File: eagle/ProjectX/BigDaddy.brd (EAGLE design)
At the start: 100 x 100 mm, 4 parts, among them U1 TC4427AEOA

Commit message: Working on the big board
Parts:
- added C1, C3, C5, C6: (no value), resistor:C0805
- added SP10, SP11, SP12, SP5, SP6, SP9: MA40S4S, Parts:MA40
- added U3, U5, U6: TC4427AEOA, Parts:SOIC127P600X175-8N
- moved U1 42.1 mm to (38.5, 36.0)
- moved SP1 41.4 mm to (43.0, 36.0), flipped to the bottom
- moved SP2 40.5 mm to (31.0, 36.0), flipped to the bottom
- moved DIP1 16.2 mm to (49.0, 54.0)
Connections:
- new net N$10: SP6.+, U3.5
- new net N$13: SP11.+, U6.7
- new net N$14: SP12.+, U6.5
- new net N$7: SP9.+, U5.7
- new net N$8: SP10.+, U5.5
- new net N$9: SP5.+, U3.7
- new net VDD: C1.2, C3.2, C5.2, C6.2, U1.6, U3.6, U5.6, U6.6
- net +5V: no longer U1.6
- net GND: now also C1.1, C3.1, C5.1, C6.1, SP10.-, SP11.-, SP12.-, SP5.-, SP6.-, SP9.-, U3.3, U5.3, U6.3
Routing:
- net GND: track 0.00 -> 32.1 mm, vias 0 -> 1
- net VDD: track 0.00 -> 26.8 mm, vias 0 -> 4
- net N$9: track 0.00 -> 8.37 mm
- net N$13: track 0.00 -> 7.58 mm
- net N$2: track 0.00 -> 5.73 mm
- net N$8: track 0.00 -> 4.73 mm
- added copper zone on layer 1, net GND
- added copper zone on layer 16, net VDD

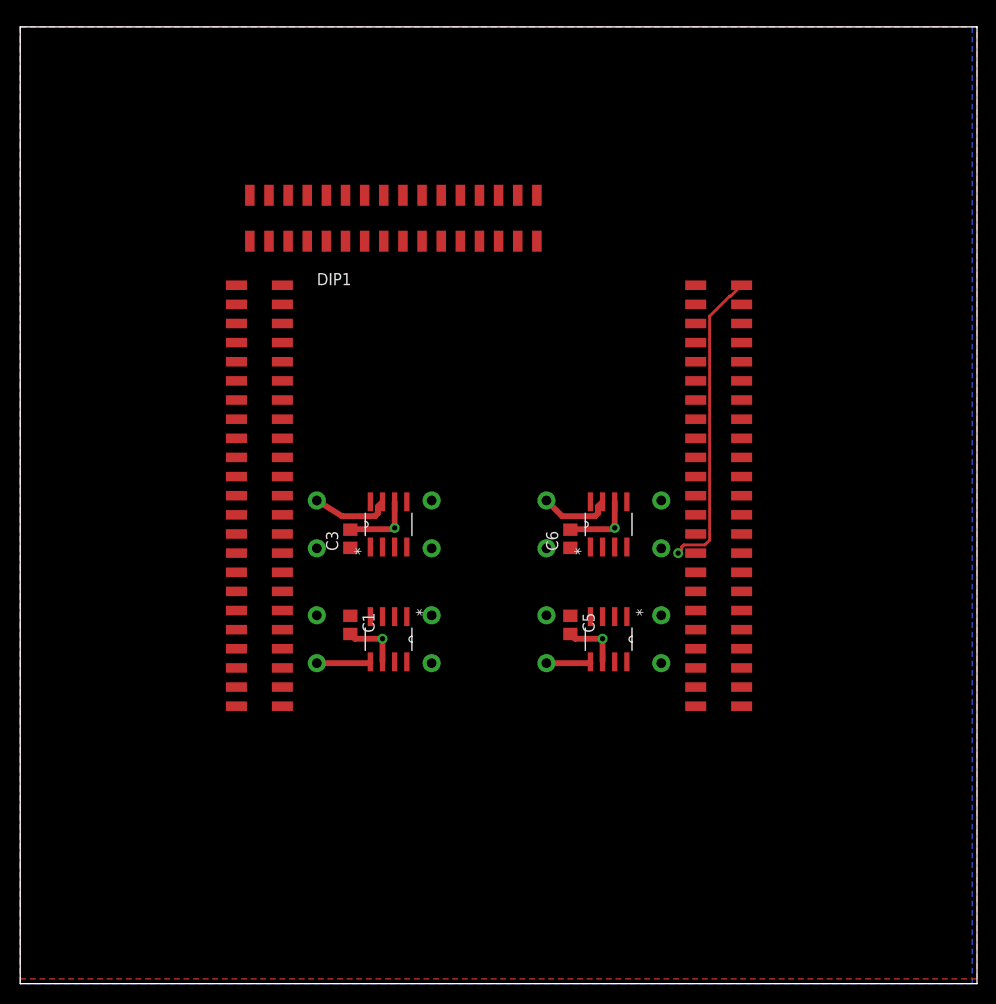
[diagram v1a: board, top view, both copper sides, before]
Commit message: Layout of transducers complete, need to add connectors, power, and then route everything
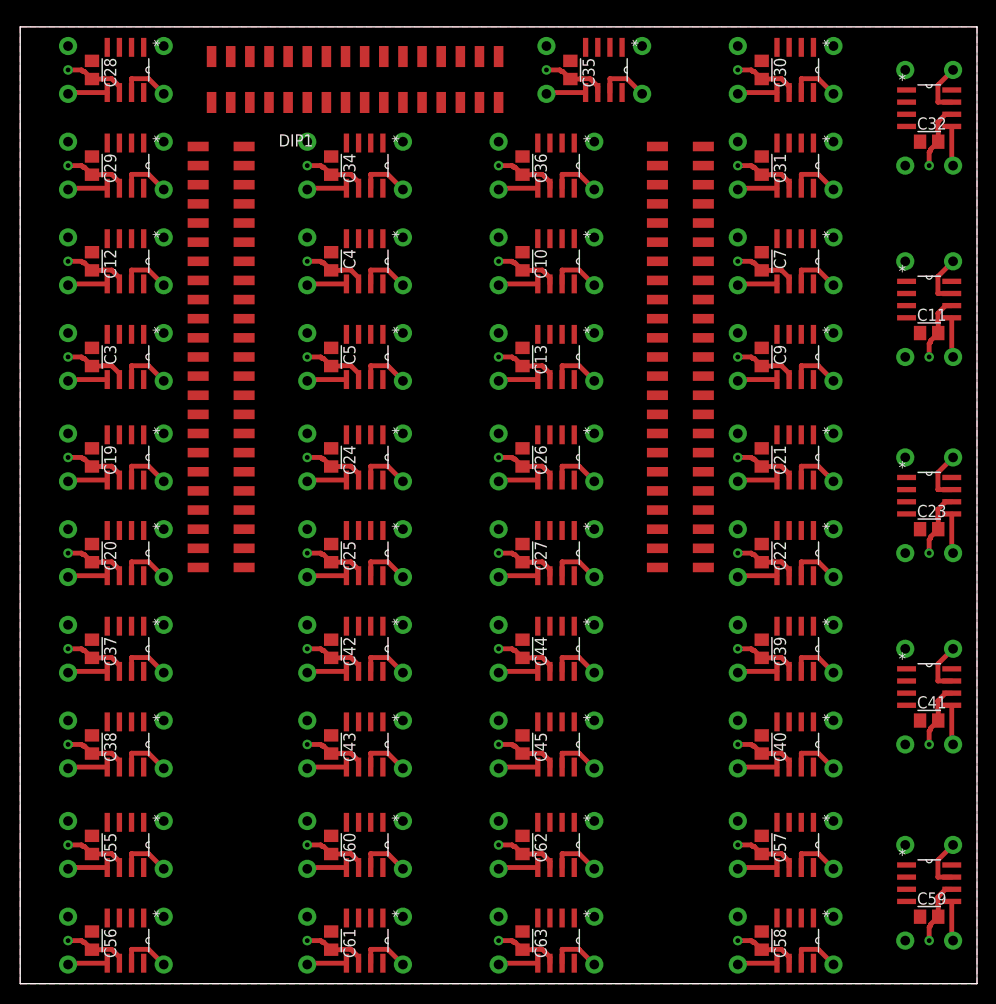
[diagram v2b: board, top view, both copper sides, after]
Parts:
- removed C1, C6: (no value), resistor:C0805
- removed SP1, SP11, SP12, SP2: MA40S4S, Parts:MA40
- removed U1, U6: TC4427AEOA, Parts:SOIC127P600X175-8N
- added C10, C11, C12, C13, C19, C20, C21, C22, C23, C24, C25, C26, C27, C28, C29, C30, C31, C32, C34, C35, C36, C37, C38, C39, C4, C40, C41, C42, C43, C44, C45, C55, C56, C57, C58, C59, C60, C61, C62, C63, C7, C9: (no value), resistor:C0805
- added SP109, SP110, SP111, SP112, SP113, SP114, SP115, SP116, SP117, SP118, SP119, SP120, SP121, SP122, SP123, SP124, SP125, SP126, SP13, SP14, SP17, SP18, SP19, SP20, SP21, SP22, SP23, SP24, SP25, SP26, SP37, SP38, SP39, SP40, SP41, SP42, SP43, SP44, SP45, SP46, SP47, SP48, SP49, SP50, SP51, SP52, SP53, SP54, SP55, SP56, SP57, SP58, SP59, SP60, SP61, SP62, SP63, SP64, SP67, SP68, SP69, SP7, SP70, SP71, SP72, SP73, SP74, SP75, SP76, SP77, SP78, SP79, SP8, SP80, SP81, SP82, SP83, SP84, SP85, SP86, SP87, SP88, SP89, SP90: MA40S4S, Parts:MA40
- added U10, U11, U12, U13, U19, U20, U21, U22, U23, U24, U25, U26, U27, U28, U29, U30, U31, U32, U34, U35, U36, U37, U38, U39, U4, U40, U41, U42, U43, U44, U45, U55, U56, U57, U58, U59, U60, U61, U62, U63, U7, U9: TC4427AEOA, Parts:SOIC127P600X175-8N
- moved SP6 41.8 mm to (5.00, 65.5), turned to 270 degrees
- moved SP9 40.0 mm to (40.0, 65.5)
- moved U5 39.0 mm to (36.0, 65.5)
- moved SP10 38.7 mm to (30.0, 65.5)
- moved C5 37.5 mm to (32.5, 65.5)
- moved C3 33.0 mm to (7.50, 65.5), turned to 270 degrees
- moved U3 32.6 mm to (11.0, 65.5), turned to 270 degrees
- moved SP5 23.7 mm to (15.0, 65.5), turned to 270 degrees
- moved DIP1 15.0 mm to (45.0, 68.5)
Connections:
- removed net N$1: SP1.+, U1.7
- removed net N$13: SP11.+, U6.7
- removed net N$14: SP12.+, U6.5
- removed net N$2: SP2.+, U1.5
- new net N$111: SP109.+, U55.7
- new net N$112: SP110.+, U55.5
- new net N$113: SP111.+, U56.7
- new net N$114: SP112.+, U56.5
- new net N$115: SP113.+, U57.7
- new net N$116: SP114.+, U57.5
- new net N$117: SP115.+, U58.7
- new net N$118: SP116.+, U58.5
- new net N$119: SP117.+, U59.7
- new net N$120: SP118.+, U59.5
- new net N$121: SP119.+, U60.7
- new net N$122: SP120.+, U60.5
- new net N$123: SP121.+, U61.7
- new net N$124: SP122.+, U61.5
- new net N$125: SP123.+, U62.7
- new net N$126: SP124.+, U62.5
- new net N$127: SP125.+, U63.7
- new net N$128: SP126.+, U63.5
- new net N$15: SP13.+, U7.7
- new net N$16: SP14.+, U7.5
- new net N$19: SP17.+, U9.7
- new net N$20: SP18.+, U9.5
- new net N$21: SP19.+, U10.7
- new net N$22: SP20.+, U10.5
- new net N$23: SP21.+, U11.7
- new net N$24: SP22.+, U11.5
- new net N$25: SP23.+, U12.7
- new net N$26: SP24.+, U12.5
- new net N$27: SP25.+, U13.7
- new net N$28: SP26.+, U13.5
- new net N$39: SP37.+, U19.7
- new net N$40: SP38.+, U19.5
- new net N$41: SP39.+, U20.7
- new net N$42: SP40.+, U20.5
- new net N$43: SP41.+, U21.7
- new net N$44: SP42.+, U21.5
- new net N$45: SP43.+, U22.7
- new net N$46: SP44.+, U22.5
- new net N$47: SP45.+, U23.7
- new net N$48: SP46.+, U23.5
- new net N$49: SP47.+, U24.7
- new net N$50: SP48.+, U24.5
- new net N$51: SP49.+, U25.7
- new net N$52: SP50.+, U25.5
- new net N$53: SP51.+, U26.7
- new net N$54: SP52.+, U26.5
- new net N$55: SP53.+, U27.7
- new net N$56: SP54.+, U27.5
- new net N$57: SP55.+, U28.7
- new net N$58: SP56.+, U28.5
- new net N$59: SP57.+, U29.7
- new net N$60: SP58.+, U29.5
- new net N$61: SP59.+, U30.7
- new net N$62: SP60.+, U30.5
- new net N$63: SP61.+, U31.7
- new net N$64: SP62.+, U31.5
- new net N$65: SP63.+, U32.7
- new net N$66: SP64.+, U32.5
- new net N$69: SP67.+, U34.7
- new net N$7: SP7.+, U4.7
- new net N$70: SP68.+, U34.5
- new net N$71: SP69.+, U35.7
- new net N$72: SP70.+, U35.5
- new net N$73: SP71.+, U36.7
- new net N$74: SP72.+, U36.5
- new net N$75: SP73.+, U37.7
- new net N$76: SP74.+, U37.5
- new net N$77: SP75.+, U38.7
- new net N$78: SP76.+, U38.5
- new net N$79: SP77.+, U39.7
- new net N$8: SP8.+, U4.5
- new net N$80: SP78.+, U39.5
- new net N$81: SP79.+, U40.7
- new net N$82: SP80.+, U40.5
- new net N$83: SP81.+, U41.7
- new net N$84: SP82.+, U41.5
- new net N$85: SP83.+, U42.7
- new net N$86: SP84.+, U42.5
- new net N$87: SP85.+, U43.7
- new net N$88: SP86.+, U43.5
- new net N$89: SP87.+, U44.7
- new net N$90: SP88.+, U44.5
- new net N$91: SP89.+, U45.7
- new net N$92: SP90.+, U45.5
- net GND: now also C10.1, C11.1, C12.1, C13.1, C19.1, C20.1, C21.1, C22.1, C23.1, C24.1, C25.1, C26.1, C27.1, C28.1, C29.1, C30.1, C31.1, C32.1, C34.1, C35.1, C36.1, C37.1, C38.1, C39.1, C4.1, C40.1, C41.1, C42.1, C43.1, C44.1, C45.1, C55.1, C56.1, C57.1, C58.1, C59.1, C60.1, C61.1, C62.1, C63.1, C7.1, C9.1, SP109.-, SP110.-, SP111.-, SP112.-, SP113.-, SP114.-, SP115.-, SP116.-, SP117.-, SP118.-, SP119.-, SP120.-, SP121.-, SP122.-, SP123.-, SP124.-, SP125.-, SP126.-, SP13.-, SP14.-, SP17.-, SP18.-, SP19.-, SP20.-, SP21.-, SP22.-, SP23.-, SP24.-, SP25.-, SP26.-, SP37.-, SP38.-, SP39.-, SP40.-, SP41.-, SP42.-, SP43.-, SP44.-, SP45.-, SP46.-, SP47.-, SP48.-, SP49.-, SP50.-, SP51.-, SP52.-, SP53.-, SP54.-, SP55.-, SP56.-, SP57.-, SP58.-, SP59.-, SP60.-, SP61.-, SP62.-, SP63.-, SP64.-, SP67.-, SP68.-, SP69.-, SP7.-, SP70.-, SP71.-, SP72.-, SP73.-, SP74.-, SP75.-, SP76.-, SP77.-, SP78.-, SP79.-, SP8.-, SP80.-, SP81.-, SP82.-, SP83.-, SP84.-, SP85.-, SP86.-, SP87.-, SP88.-, SP89.-, SP90.-, U10.3, U11.3, U12.3, U13.3, U19.3, U20.3, U21.3, U22.3, U23.3, U24.3, U25.3, U26.3, U27.3, U28.3, U29.3, U30.3, U31.3, U32.3, U34.3, U35.3, U36.3, U37.3, U38.3, U39.3, U4.3, U40.3, U41.3, U42.3, U43.3, U44.3, U45.3, U55.3, U56.3, U57.3, U58.3, U59.3, U60.3, U61.3, U62.3, U63.3, U7.3, U9.3; no longer C1.1, C6.1, SP1.-, SP11.-, SP12.-, SP2.-, U1.3, U6.3
- net VDD: now also C10.2, C11.2, C12.2, C13.2, C19.2, C20.2, C21.2, C22.2, C23.2, C24.2, C25.2, C26.2, C27.2, C28.2, C29.2, C30.2, C31.2, C32.2, C34.2, C35.2, C36.2, C37.2, C38.2, C39.2, C4.2, C40.2, C41.2, C42.2, C43.2, C44.2, C45.2, C55.2, C56.2, C57.2, C58.2, C59.2, C60.2, C61.2, C62.2, C63.2, C7.2, C9.2, U10.6, U11.6, U12.6, U13.6, U19.6, U20.6, U21.6, U22.6, U23.6, U24.6, U25.6, U26.6, U27.6, U28.6, U29.6, U30.6, U31.6, U32.6, U34.6, U35.6, U36.6, U37.6, U38.6, U39.6, U4.6, U40.6, U41.6, U42.6, U43.6, U44.6, U45.6, U55.6, U56.6, U57.6, U58.6, U59.6, U60.6, U61.6, U62.6, U63.6, U7.6, U9.6; no longer C1.2, C6.2, U1.6, U6.6
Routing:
- net VDD: track 26.8 -> 297.1 mm, vias 4 -> 44
- net GND: track 32.1 -> 0.00 mm, vias 1 -> 0
- net N$13: track 7.58 -> 0.00 mm
- net N$2: track 5.73 -> 0.00 mm
- net N$91: track 0.00 -> 5.47 mm
- net N$9: track 0.00 -> 5.47 mm
- net N$89: track 0.00 -> 5.47 mm
- net N$87: track 0.00 -> 5.47 mm
- net N$85: track 0.00 -> 5.47 mm
- net N$73: track 0.00 -> 5.47 mm
- net N$71: track 0.00 -> 5.47 mm
- net N$7: track 0.00 -> 5.47 mm
- net N$69: track 0.00 -> 5.47 mm
- net N$55: track 0.00 -> 5.47 mm
- net N$53: track 0.00 -> 5.47 mm
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
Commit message: Some fixes to placement
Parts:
- added J1: (no value), SparkFun-Connectors:1X02_LOCK_LONGPADS
- moved C10 0.50 mm to (52.5, 75.0)
- moved C11 0.50 mm to (95.0, 67.5)
- moved C12 0.50 mm to (7.50, 75.0)
- moved C13 0.50 mm to (52.5, 65.0)
- moved C28 0.50 mm to (7.50, 95.0)
- moved C29 0.50 mm to (7.50, 85.0)
- moved C3 0.50 mm to (7.50, 65.0)
- moved C30 0.50 mm to (77.5, 95.0)
- moved C31 0.50 mm to (77.5, 85.0)
- moved C32 0.50 mm to (95.0, 87.5)
- moved C34 0.50 mm to (32.5, 85.0)
- moved C35 0.50 mm to (57.5, 95.0)
- moved C36 0.50 mm to (52.5, 85.0)
- moved C4 0.50 mm to (32.5, 75.0)
- moved C5 0.50 mm to (32.5, 65.0)
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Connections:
- net +5V: now also DIP1.5V@1
- net GND: now also J1.2
- net VDD: now also J1.1

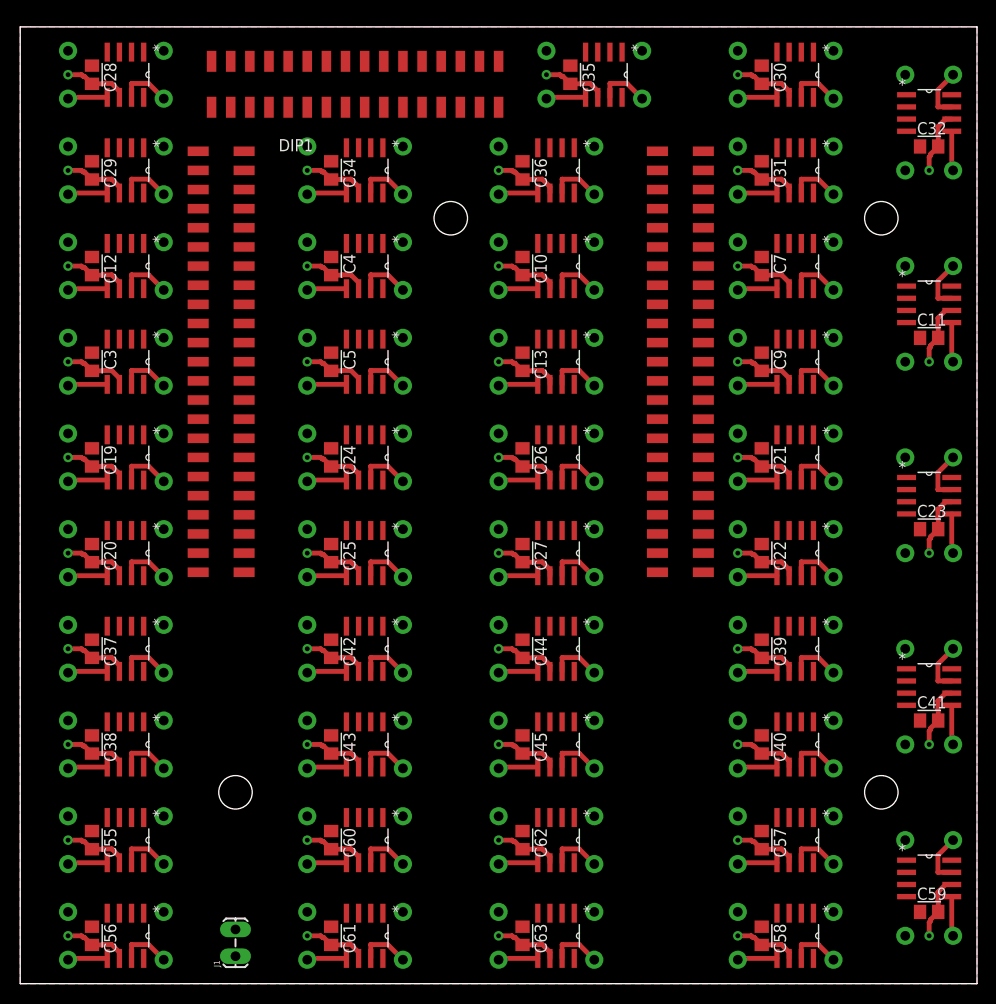
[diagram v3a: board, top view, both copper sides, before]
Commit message: Ready to route signal traces
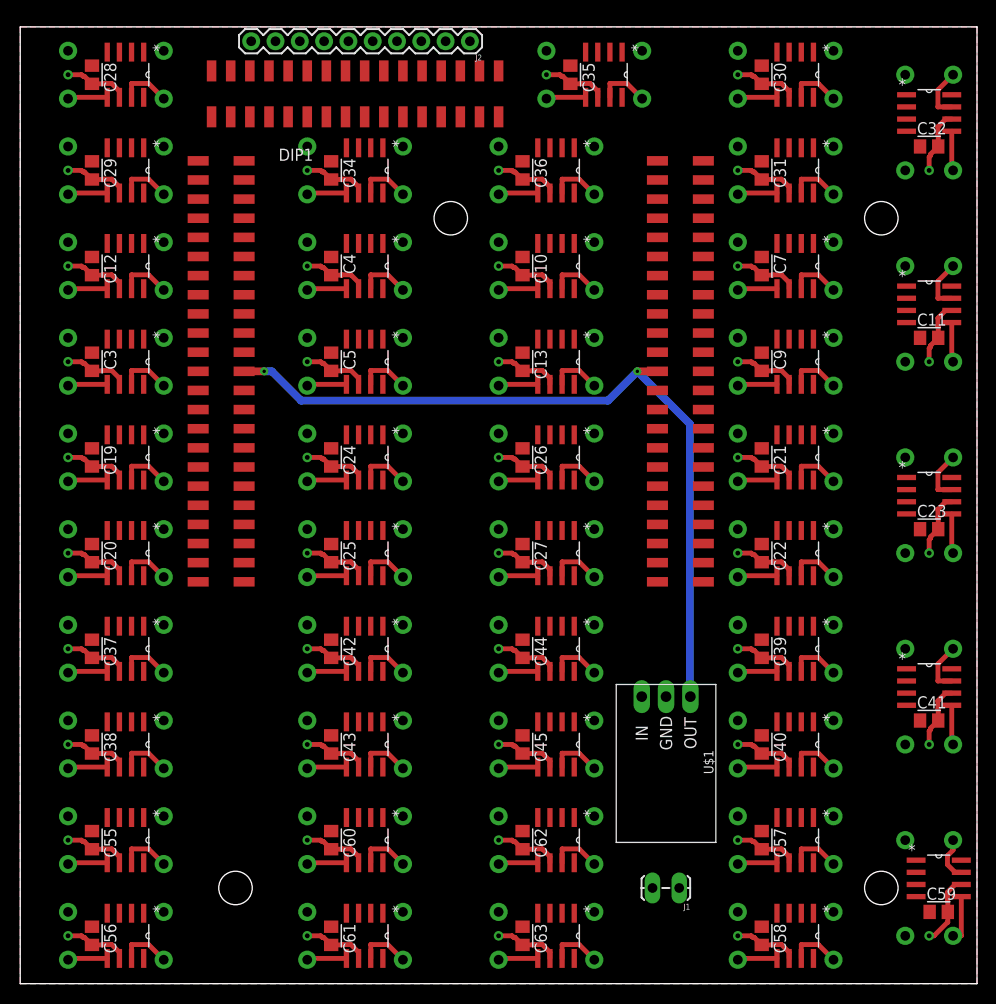
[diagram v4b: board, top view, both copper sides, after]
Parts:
- added J2: (no value), SparkFun-Connectors:1X10
- added U$1: OKI-78SR, Parts:OKI-78SR-HORIZ
- moved J1 46.8 mm to (68.8, 10.0), turned to 180 degrees
- moved C59 1.00 mm to (96.0, 7.50)
- moved DIP1 1.00 mm to (45.0, 67.0)
- moved U59 1.00 mm to (96.0, 11.0)
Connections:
- net +5V: now also U$1.OUT
- net GND: now also U$1.GND
- net VDD: now also U$1.IN
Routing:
- net +5V: track 0.00 -> 82.0 mm, vias 0 -> 2
- net N$119: track 5.47 -> 4.59 mm
- net N$120: track 4.23 -> 5.10 mm
- net VDD: track 297.1 -> 297.8 mm
